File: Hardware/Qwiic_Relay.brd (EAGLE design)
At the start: 25.4 x 50.8 mm, 47 parts, among them J4 AVR_SPI_PROG_3X2TESTPOINTS, K1 RELAY-SPDT, Q4 600mA/40V, U1 ATTINY85_SOIC_5.3MM, U2 LTV-816_OPTO_ISOLATOR"

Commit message: pre review
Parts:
- added U$15: (no value), buzzard_labels (10):20
- added U$16: (no value), buzzard_labels (10):I__C1
- R6, R7: value 2.2K -> 2.2k
- R8: value 10K -> 10k
- moved JP6 24.1 mm to (24.8, 0.64)
- moved JP2 24.0 mm to (0.76, 50.2)
- moved R6 2.54 mm to (17.8, 47.0), turned to 180 degrees
- moved R7 2.54 mm to (7.62, 47.0), turned to 0 degrees
- moved LOGO1 1.02 mm to (2.41, 6.35), turned to 270 degrees
- moved C1 0.63 mm to (7.62, 45.1)
- moved R8 0.63 mm to (17.8, 45.1)
- moved U$3 0.51 mm to (2.79, 20.3), turned to 90 degrees
- moved U$4 0.51 mm to (2.79, 20.3), turned to 270 degrees
- moved U$2 0.38 mm to (-0.89, 6.35)
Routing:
- net GND: track 24.1 -> 0.00 mm, vias 4 -> 5
- net 3.3V: track 75.2 -> 59.6 mm, vias 3 -> 5
- net SDA: track 46.0 -> 40.9 mm
- net SCL: track 26.2 -> 27.8 mm
- net N$4: track 1.88 -> 3.27 mm
- net N$10: track 1.88 -> 3.27 mm
- net !RESET: track 12.2 -> 11.6 mm, vias 1 -> 0
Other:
- board text added: "v10"
- board text removed: "v01"

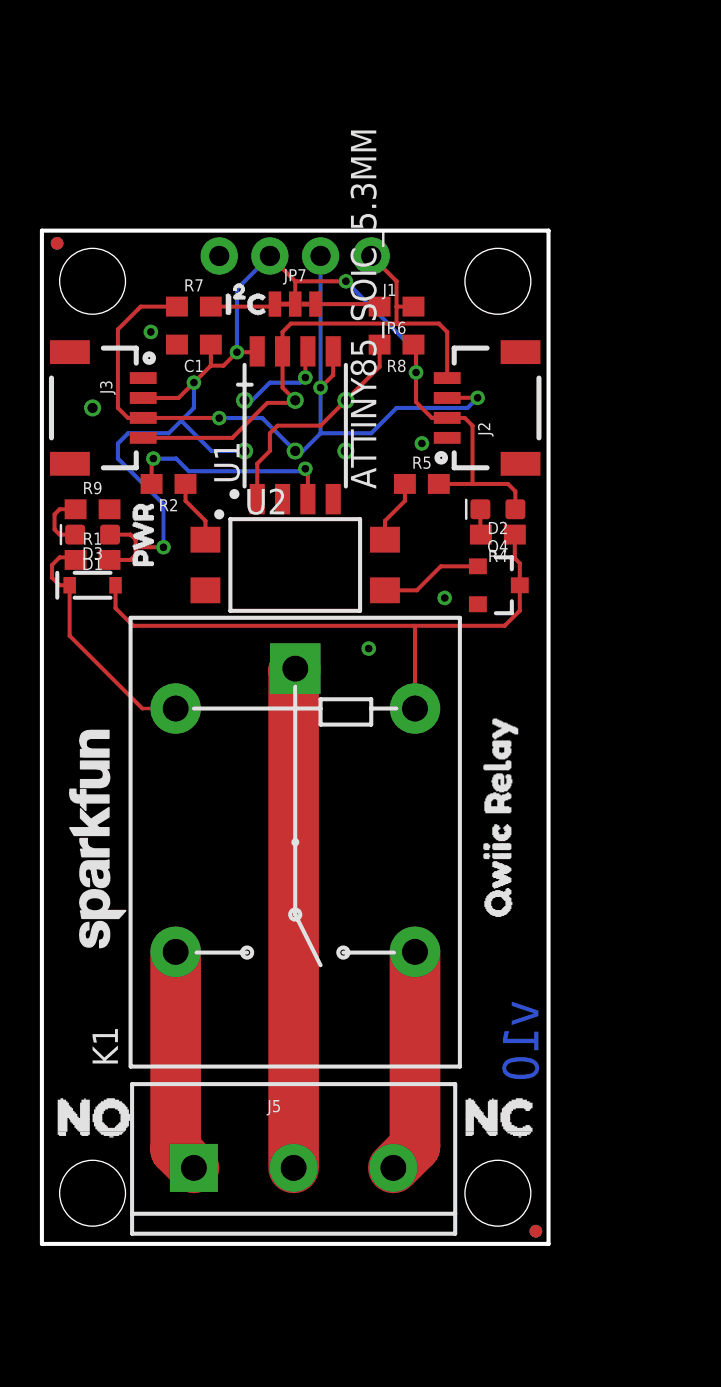
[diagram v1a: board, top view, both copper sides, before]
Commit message: changing to most recent rev
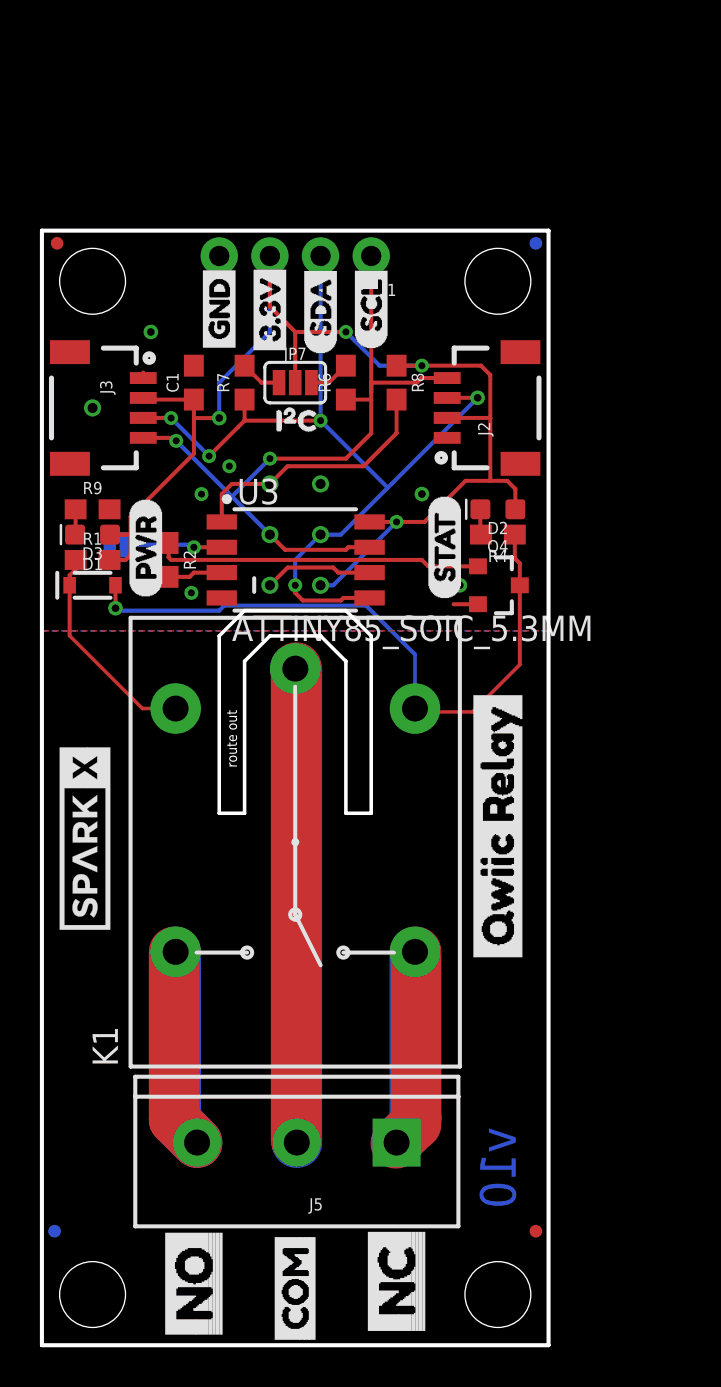
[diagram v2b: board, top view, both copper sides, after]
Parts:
- removed LOGO2: REVISION, SparkFun-Aesthetics:REVISION
- removed R5: 330, SparkFun-Resistors:0603
- removed U$10: (no value), buzzard_labels (6):SCL3
- removed U1: ATTINY85_SOIC_5.3MM, SparkFun-IC-Microcontroller:ATTINY85
- removed U2: LTV-816_OPTO_ISOLATOR", SparkFun-DiscreteSemi:LTV-816_4PIN_DIP
- added JP10: JUMPER-SMT_2_NO_NO-SILK, SparkFun-Jumpers:SMT-JUMPER_2_NO_NO-SILK
- added U$17, U$20: (no value), buzzard_labels:NC3
- added U$18: (no value), buzzard_labels:NO2
- added U$19: (no value), buzzard_labels:COM4
- added U$21: (no value), buzzard_labels (10):20
- added U$22: (no value), Labels-0_04:3.3V
- added U$23: (no value), buzzard_labels (11):SCL1
- added U$24: (no value), buzzard_labels (11):SDA0
- added U$25: (no value), buzzard_labels (12):STAT1
- added U3: ATTINY85_SOIC_5.3MM, SparkFun-IC-Microcontroller:ATTINY85
- JP7: value JUMPER-SMT_3_2-NC_TRACE_NO-SILK -> (none); device SparkFun-Jumpers:SMT-JUMPER_3_2-NC_TRACE_NO-SILK -> SparkFun-Jumpers:SMT-JUMPER_3_2-NC_PASTE_SILK
- K1: value RELAY-SPDT -> (none); device SparkFun-Electromechanical:RELAY_G5LE -> SparkX:RELAY_SPDT_1C
- R2: value 100 -> 330
- U$1: device buzzard_labels (4):NC1 -> Labels:QWIIC-LOGO-MEDIUM
- U$11: device buzzard_labels (6):SDA2 -> buzzard_labels:NO2
- U$12: device buzzard_labels (4):NC1 -> buzzard_labels (1):COM7
- U$13: device buzzard_labels (4):NO0 -> Labels-0_04:GND
- U$14: device buzzard_labels (8):COM3 -> buzzard_labels (10):I__C1
- U$15: device buzzard_labels (10):20 -> buzzard_labels:QWIIC_RELAY1
- U$16: device buzzard_labels (10):I__C1 -> buzzard_labels:QWIIC_RELAY1
- U$2: device buzzard_labels (4):NO0 -> Labels-0_04:(PWR)
- U$3, U$4: value SFE_LOGO_NAME.1_INCH -> SPARKX-LOGO4; device SparkFun-Aesthetics:SFE_LOGO_NAME_.1 -> SparkX:SPARKX-MEDIUM
- U$5: device buzzard_labels (4):PWR2 -> Labels-0_04:SCL
- U$6: device buzzard_labels (5):QWIIC_RELAY2 -> Labels-0_04:SDA
- U$7: device buzzard_labels (5):QWIIC_RELAY2 -> Labels-0_04:3.3V
- U$8: device buzzard_labels (6):3V31 -> Labels-0_04:GND
- U$9: device buzzard_labels (6):GND0 -> Labels-0_04:(ADR)
- moved U$11 50.4 mm to (7.62, -5.46), flipped to the top
- moved U$13 39.5 mm to (8.89, 44.5), flipped to the top
- moved U$15 36.9 mm to (22.9, 13.6), turned to 90 degrees
- moved U$14 36.4 mm to (10.8, 41.3), flipped to the top, turned to 0 degrees
- moved U$6 35.2 mm to (14.0, 49.3), flipped to the bottom, turned to 270 degrees
- moved U$2 26.7 mm to (5.21, 32.4), turned to 90 degrees
- moved FRAME1 26.5 mm to (10.2, -16.5)
- moved U$7 24.9 mm to (11.4, 49.3)
- moved JP6 24.1 mm to (0.64, 0.64)
- moved JP2 24.0 mm to (24.8, 50.2)
- moved U$16 23.8 mm to (22.9, 28.3), flipped to the bottom, turned to 270 degrees
- moved U$5 19.9 mm to (16.5, 49.3), flipped to the bottom, turned to 270 degrees
- moved U$12 11.6 mm to (12.7, -5.46), flipped to the top
- moved U$9 10.2 mm to (1.52, 37.3), turned to 270 degrees
- moved J5 10.2 mm to (17.8, 5.08), turned to 180 degrees
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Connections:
- removed net N$3: R2.1, U2.1
- removed net N$9: R5.1, U2.4
- new net N$5: JP10.1, U3.2
- net !RESET: now also U3.1; no longer U1.1
- net 3.3V: now also U3.8; no longer R5.2, U1.8
- net GND: now also JP10.2, U3.4; no longer U1.4, U2.2
- net MISO: now also U3.6; no longer U1.6
- net N$1: now also R2.1; no longer U2.3
- net NC: now also J5.1; no longer J5.3
- net NO: now also J5.3; no longer J5.1
- net RELAY_CTR: now also U3.3; no longer U1.3
- net SCL: now also U3.7; no longer U1.7
- net SDA: now also U3.5; no longer U1.5
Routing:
- net COM: track 25.1 -> 71.3 mm
- net NC: track 11.3 -> 38.1 mm
- net N$1: track 5.16 -> 16.4 mm
- net SCL: track 27.8 -> 36.6 mm, vias 0 -> 2
- net NO: track 11.2 -> 20.0 mm
- net RELAY_CTR: track 10.8 -> 2.76 mm, vias 2 -> 0
- net 3.3V: track 59.6 -> 65.9 mm, vias 5 -> 4
- net N$5: track 0.00 -> 4.85 mm, vias 0 -> 1
- net SDA: track 40.9 -> 45.4 mm, vias 3 -> 5
- net N$9: track 3.21 -> 0.00 mm
- net N$3: track 3.21 -> 0.00 mm
- net N$2: track 30.2 -> 33.0 mm, vias 0 -> 1
- net N$13: track 3.06 -> 1.28 mm
- net !RESET: track 11.6 -> 13.1 mm
- net GND: track 0.00 -> 1.50 mm, vias 5 -> 7
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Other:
- board size 25.4 x 50.8 mm -> 25.4 x 55.9 mm
- board text added: "3 Pin 5mm Screw Terminal"
- board text added: "3V Relay"
- board text added: "ATTiny85"
- board text added: "Max Current 5.5A @ 240VAC 100 mil width 15 *C Rise 1 Oz Cu"
- board text added: "http://www.sphere.bc.ca/class/downloads/ipc_2221a-pcb%20standards.pdf Table 6-1 : Electrical Conductor Spacing 6.3.2 B2-External conductors, Uncoated, Seal Level to 3050 m 300 to 500 V below 3050 m 2.5 mm >= Clearance"
- board text added: "route out"
- board text removed: "Andy England"
- board text removed: "Max Current 5.5A 100 mil width 15 *C Rise 1 Oz Cu"

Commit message: pre review
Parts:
- added LOGO2: REVISION, SparkFun-Aesthetics:REVISION
- added U$10: (no value), SparkFun-Aesthetics:ORDERING_INSTRUCTIONS
- added U$26: (no value), buzzard_labels (13):WARNING#_HIGH_VOLTAGE0
- JP7: value (none) -> JUMPER-SMT_3_2-NC_TRACE_NO-SILK; device SparkFun-Jumpers:SMT-JUMPER_3_2-NC_PASTE_SILK -> SparkFun-Jumpers:SMT-JUMPER_3_2-NC_TRACE_NO-SILK
- K1: value (none) -> RELAY-SPDT; device SparkX:RELAY_SPDT_1C -> SparkFun-Electromechanical:RELAY_G5LE
- U$3: value SPARKX-LOGO4 -> SFE_LOGO_NAME.1_INCH; device SparkX:SPARKX-MEDIUM -> SparkFun-Aesthetics:SFE_LOGO_NAME_.1
- U$4: value SPARKX-LOGO4 -> SFE_LOGO_NAME_FLAME.1_INCH; device SparkX:SPARKX-MEDIUM -> SparkFun-Aesthetics:SFE_LOGO_NAME_FLAME_.1
- moved FRAME1 27.7 mm to (-16.5, -8.89)
- moved JP2 24.8 mm to (0.76, 56.5)
- moved JP6 24.7 mm to (24.8, 5.71)
- moved U$25 7.62 mm to (20.1, 39.9)
- moved C1 6.35 mm to (7.62, 49.5)
- moved D2 6.35 mm to (22.9, 43.2)
- moved J1 6.35 mm to (16.5, 55.9)
- moved J2 6.35 mm to (20.3, 48.3)
- moved J3 6.35 mm to (5.08, 48.3)
- moved JP10 6.35 mm to (3.81, 41.4)
- moved JP3 6.35 mm to (2.54, 54.6)
- moved JP4 6.35 mm to (22.9, 54.6)
- moved JP7 6.35 mm to (12.7, 49.5)
- moved JP9 6.35 mm to (0.76, 56.5)
- moved R1 6.35 mm to (2.54, 40.6)
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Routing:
- net COM: track 71.3 -> 23.8 mm
- net N$1: track 16.4 -> 22.3 mm, vias 0 -> 2
- net N$2: track 33.0 -> 35.3 mm
- net GND: track 1.50 -> 0.00 mm
- net SDA: track 45.4 -> 44.4 mm
- net SCL: track 36.6 -> 36.1 mm
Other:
- board size 25.4 x 55.9 mm -> 25.4 x 57.1 mm
- board text added: "2 Oz. Copper"
- board text added: "Andy England"
- board text added: "Max Current 5.5A @ 240VAC 100 mil width 15 *C Rise 2 Oz Cu"
- board text removed: "Max Current 5.5A @ 240VAC 100 mil width 15 *C Rise 1 Oz Cu"

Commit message: post review
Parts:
- added U$27: (no value), buzzard_labels (15):HV2
- added U$28: (no value), buzzard_labels (15):LV1
- U$15, U$16: device buzzard_labels:QWIIC_RELAY1 -> buzzard_labels (15):_QWIIC_RELAY0
- U3: value ATTINY85_SOIC_5.3MM -> ATTINY85
- moved U$15 3.81 mm to (22.9, 14.9)
- moved U$1 1.27 mm to (21.6, 14.0)
- moved R2 0.76 mm to (7.11, 40.6)
- moved U$2 0.65 mm to (5.08, 39.4)
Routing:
- net N$5: track 4.85 -> 8.26 mm
- net RELAY_CTR: track 2.76 -> 1.99 mm
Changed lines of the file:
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@@
 <attribute name="VALUE" value="10" x="-1.143" y="40.894" size="0.6096" layer="27" font="vector" ratio="20" align="top-center"/>
 </element>
-<element name="R2" library="SparkFun-Resistors" package="0603" value="330" x="6.35" y="40.64" rot="R270">
-<attribute name="PROD_ID" value="RES-00818" x="6.35" y="40.64" size="1.778" layer="27" rot="R270" display="off"/>
+<element name="R2" library="SparkFun-Resistors" package="0603" value="330" x="7.112" y="40.64" rot="R270">
+<attribute name="PROD_ID" value="RES-00818" x="7.112" y="40.64" size="1.778" layer="27" rot="R270" display="off"/>
 </element>
 <element name="R4" library="SparkFun-Resistors" package="0603" value="330" x="22.86" y="41.91" smashed="yes" rot="R180">
@@
 <attribute name="PROD_ID" value="CONN-09696" x="16.51" y="55.88" size="1.778" layer="27" font="vector" ratio="15" rot="R180" display="off"/>
 </element>
-<element name="U$2" library="Labels-0_04" package="(PWR)" value="" x="5.207" y="38.735" rot="R90"/>
+<element name="U$2" library="Labels-0_04" package="(PWR)" value="" x="5.08" y="39.37" rot="R90"/>
 <element name="U$5" library="Labels-0_04" package="SCL" value="" x="16.51" y="55.626" rot="MR270"/>
 <element name="U$6" library="Labels-0_04" package="SDA" value="" x="13.97" y="55.626" rot="MR270"/>
 <element name="U$7" library="Labels-0_04" package="3.3V" value="" x="11.43" y="55.626" rot="MR270"/>
 <element name="U$8" library="Labels-0_04" package="GND" value="" x="8.89" y="55.626" rot="MR270"/>
-<element name="U$15" library="buzzard_labels" package="QWIIC_RELAY1" value="" x="22.86" y="18.669" rot="R90"/>
-<element name="U$16" library="buzzard_labels" package="QWIIC_RELAY1" value="" x="22.86" y="33.401" rot="MR270"/>
+<element name="U$15" library="buzzard_labels (15)" package="_QWIIC_RELAY0" value="" x="22.86" y="14.859" rot="R90"/>
+<element name="U$16" library="buzzard_labels (15)" package="_QWIIC_RELAY0" value="" x="22.86" y="33.401" rot="MR270"/>
 <element name="U$17" library="buzzard_labels" package="NC3" value="" x="17.78" y="8.255" rot="MR270"/>
 <element name="U$18" library="buzzard_labels" package="NO2" value="" x="7.62" y="8.382" rot="MR270"/>
@@
 <attribute name="SF_SKU" value="PRT-08433" x="17.78" y="10.16" size="1.778" layer="27" font="vector" ratio="15" rot="R180" display="off"/>
 </element>
-<element name="U$1" library="Labels" package="QWIIC-LOGO-MEDIUM" value="" x="21.59" y="15.24" rot="MR270"/>
-<element name="U3" library="SparkFun-IC-Microcontroller" package="ATTINY85" value="ATTINY85_SOIC_5.3MM" x="12.7" y="40.64">
+<element name="U$1" library="Labels" package="QWIIC-LOGO-MEDIUM" value="" x="21.59" y="13.97" rot="MR270"/>
+<element name="U3" library="SparkFun-IC-Microcontroller" package="ATTINY85" value="ATTINY85" x="12.7" y="40.64">
 <attribute name="PROD_ID" value="IC-09092" x="12.7" y="40.64" size="1.778" layer="27" display="off"/>
 </element>
@@
 <element name="U$10" library="SparkFun-Aesthetics" package="ORDERING_INSTRUCTIONS" value="" x="-34.29" y="-13.97"/>
 <element name="U$26" library="buzzard_labels (13)" package="WARNING#_HIGH_VOLTAGE0" value="" x="12.7" y="30.48" rot="MR270"/>
+<element name="U$27" library="buzzard_labels (15)" package="HV2" value="" x="22.987" y="37.973" rot="MR270"/>
+<element name="U$28" library="buzzard_labels (15)" package="LV1" value="" x="22.987" y="43.053" rot="MR270"/>
 </elements>
 <signals>
@@
 <contactref element="U3" pad="3"/>
 <wire x1="9.01699375" y1="40.005" x2="7.62" y2="40.005" width="0.2032" layer="1"/>
-<wire x1="7.405" y1="39.79" x2="6.35" y2="39.79" width="0.2032" layer="1"/>
+<wire x1="7.405" y1="39.79" x2="7.112" y2="39.79" width="0.2032" layer="1"/>
 <wire x1="7.62" y1="40.005" x2="7.405" y2="39.79" width="0.2032" layer="1"/>
 <wire x1="9.017" y1="40.005" x2="9.01699375" y2="40.005" width="0.1778" layer="1"/>
@@
 <wire x1="20.005" y1="40.32" x2="18.796" y2="41.529" width="0.2032" layer="1"/>
 <via x="18.796" y="41.529" extent="1-16" drill="0.381"/>
-<wire x1="6.35" y1="41.49" x2="5.08" y2="40.22" width="0.2032" layer="1"/>
-<wire x1="5.08" y1="40.22" x2="5.08" y2="38.354" width="0.2032" layer="1"/>
+<wire x1="7.112" y1="41.49" x2="5.08" y2="39.458" width="0.2032" layer="1"/>
+<wire x1="5.08" y1="39.458" x2="5.08" y2="38.354" width="0.2032" layer="1"/>
 <via x="5.08" y="38.354" extent="1-16" drill="0.381"/>
 <wire x1="5.08" y1="38.354" x2="7.2120125" y2="38.354" width="0.2032" layer="16"/>
@@
 <contactref element="JP10" pad="1"/>
 <contactref element="U3" pad="2"/>
-<wire x1="7.620003125" y1="41.275" x2="9.016996875" y2="41.275" width="0.2032" layer="1"/>
-<via x="7.62" y="41.275" extent="1-16" drill="0.381"/>
-<wire x1="7.62" y1="41.275" x2="7.493" y2="41.402" width="0.2032" layer="16"/>
-<wire x1="7.493" y1="41.402" x2="4.2164" y2="41.402" width="0.2032" layer="16"/>
+<wire x1="8.890003125" y1="41.275" x2="9.016996875" y2="41.275" width="0.2032" layer="1"/>
+<via x="10.541" y="41.148" extent="1-16" drill="0.381"/>
+<wire x1="10.541" y1="41.148" x2="10.287" y2="41.402" width="0.2032" layer="16"/>
+<wire x1="10.287" y1="41.402" x2="4.2164" y2="41.402" width="0.2032" layer="16"/>
 <wire x1="9.017" y1="41.275" x2="9.016996875" y2="41.275" width="0.1778" layer="1"/>
-<wire x1="7.62" y1="41.275" x2="7.620003125" y2="41.275" width="0.1778" layer="1"/>
+<wire x1="10.541" y1="41.148" x2="10.414" y2="41.275" width="0.1778" layer="1"/>
+<wire x1="10.414" y1="41.275" x2="8.890003125" y2="41.275" width="0.1778" layer="1"/>
 </signal>
 </signals>
